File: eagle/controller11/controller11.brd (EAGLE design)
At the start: 36.8 x 64.8 mm, 62 parts, among them IC1 ILD213T, IC2 ILD213T, J2 FEMALE 2x3, Q2 200mA/50V, Q4 200mA/50V, Q5 200mA/50V, U3 MP2307, X1 1501_04, X2 ZX62D-B-5PA8

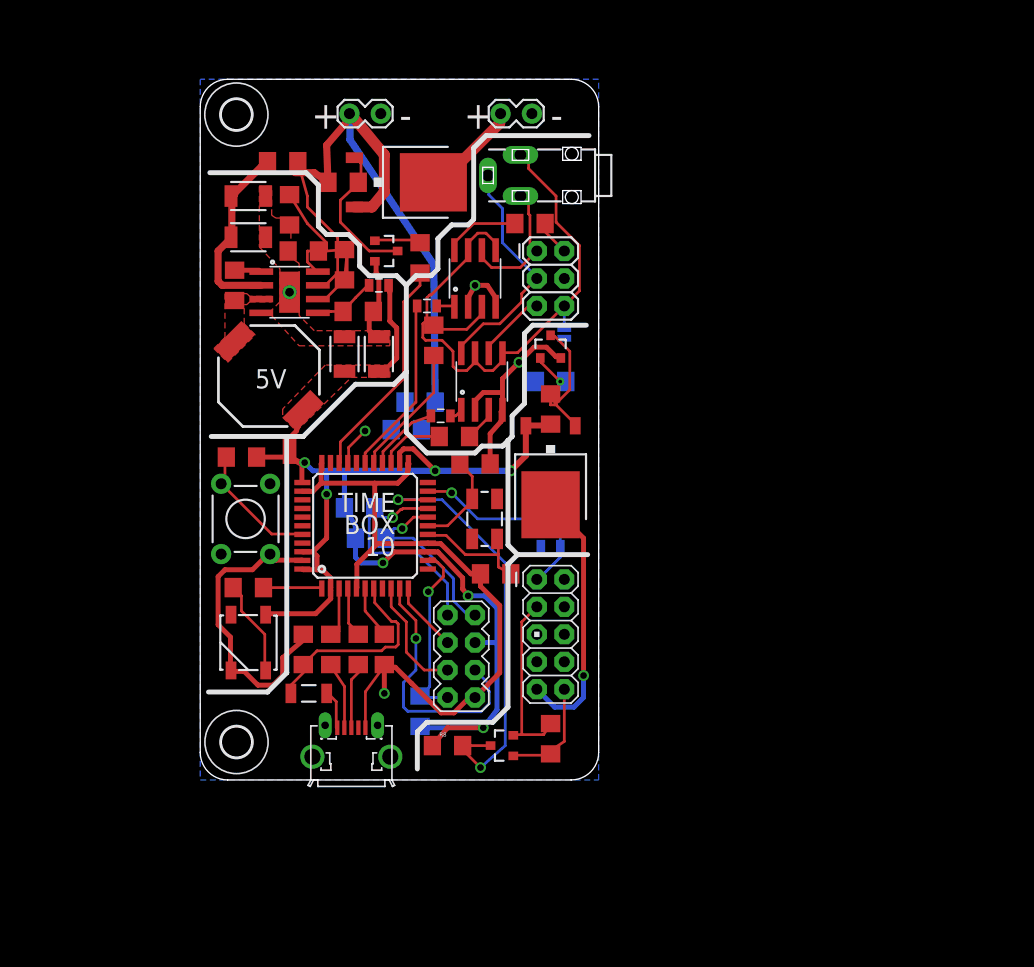
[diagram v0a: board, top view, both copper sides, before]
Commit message: controller11: new board layout
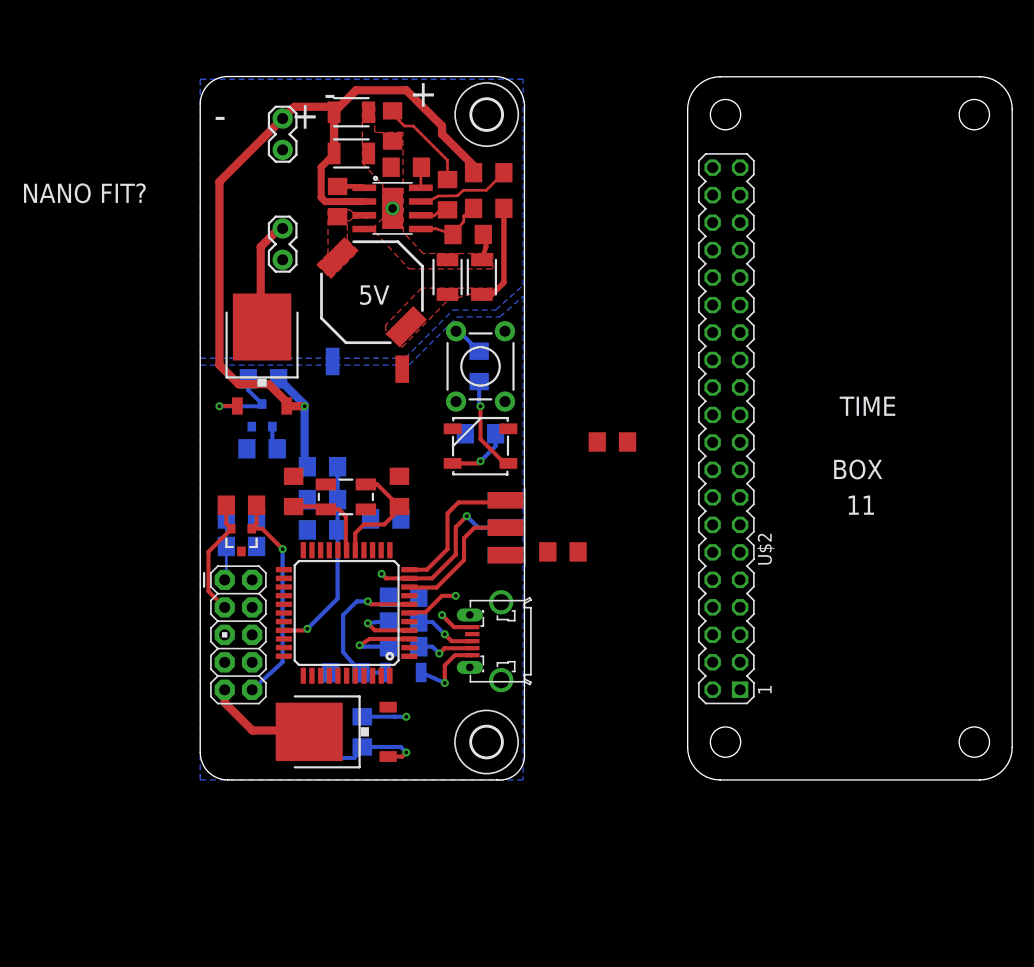
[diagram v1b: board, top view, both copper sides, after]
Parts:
- removed IC1, IC2: ILD213T, SparkFun-DiscreteSemi:SO08
- removed J2: FEMALE 2x3, SparkFun-Connectors:2X3
- removed J3: (no value), SparkFun-Connectors:2X4
- removed JP1: (no value), SparkFun-Passives:PAD-JUMPER-2-NO_YES_SILK
- removed R13, R14, R15, R16, R19: (no value), SparkFun-Passives:1206
- removed R18, R20: (no value), SparkFun-Passives:0805
- removed X1: 1501_04, con-lumberg:1501_05
- added C1, C6: 0.1uF, SparkFun-Capacitors:1206
- added SH2: SHORT-HT5, shorts:SHORT_TOP-50
- added U$1: AVR-ISP-6-EDGE, avr-6:6PAD_ISP
- added U$2: PIZERO_THROUGH_HOLE, pizero:PIZERO_THOUGH_HOLE
- R11, R12, R3: device SparkFun-Resistors:0805 -> SparkFun-Resistors:1206
- moved Q4 41.2 mm to (11.6, 4.45), flipped to the bottom, turned to 270 degrees
- moved R6 40.4 mm to (8.26, 4.45), turned to 90 degrees
- moved R7 35.8 mm to (3.81, 25.4), turned to 180 degrees
- moved R4 34.5 mm to (15.0, 4.45), flipped to the bottom, turned to 270 degrees
- moved Q5 30.7 mm to (3.81, 22.2), turned to 180 degrees
- moved Q3 30.7 mm to (12.6, 4.45), turned to 90 degrees
- moved J1 28.9 mm to (3.53, 13.4)
- moved R11 28.7 mm to (3.81, 21.6), turned to 0 degrees
- moved R12 28.7 mm to (3.81, 24.1), turned to 180 degrees
- moved D2 28.1 mm to (25.9, 30.9), turned to 180 degrees
- moved J9 26.5 mm to (7.62, 48.3), turned to 90 degrees
- moved S1 25.9 mm to (25.9, 38.2)
- moved R_LED 25.7 mm to (25.9, 32.0), flipped to the bottom
- moved R5 23.5 mm to (25.8, 38.2), flipped to the bottom, turned to 90 degrees
- moved H2 23.1 mm to (26.5, 61.5)
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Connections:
- removed net CAM3: R18.1, U$3.26
- removed net CAM4: R19.1, U$3.25
- removed net N$12: IC2.1, R18.2
- removed net N$13: IC2.3, R19.2
- removed net N$15: IC1.3, R15.2
- removed net N$16: J2.2, R13.2
- removed net N$18: IC1.8, R13.1
- removed net N$19: IC1.1, R20.2
- removed net N$31: IC1.6, J2.1, X1.3
- removed net N$32: IC2.8, J2.3, X1.2
- removed net N$33: IC2.6, J2.5
- removed net N$34: IC1.5, IC1.7, IC2.5, IC2.7, J2.6, JP1.2, X1.1
- removed net SCL: J3.2, R16.2, U$3.18
- removed net SDA: J3.1, R14.1, U$3.19
- new net FOO10: U$3.32
- new net FOO9: U$3.31
- new net GNDA: C15.1, C16.1, C17.1, C18.2, C19.1, R1.2, R2.2, SH2.1, U3.4, U3.BTM, U3.P$1
- net CAM1: no longer R20.1
- net CAM2: no longer R15.1
- net CAM_EN: now also U$3.25; no longer U$3.31
- net GND: now also C1.1, C6.2, SH2.2, U$1.GND; no longer C15.1, C16.1, C17.1, C18.2, C19.1, IC1.2, IC1.4, IC2.2, IC2.4, J3.8, JP1.1, R1.2, R2.2, U3.4, U3.BTM, U3.P$1
- net MISO: now also U$1.MISO; no longer J3.3
- net MOSI: now also U$1.MOSI; no longer J3.6
- net RST: now also U$1.RST; no longer J3.7
- net SCK: now also U$1.SCK; no longer J3.5
- net VCC: now also C1.2, U$1.VCC; no longer J3.4, R14.2, R16.1
- net VD_DIRECT: now also C6.1
- net ZERO_EN: now also U$3.26; no longer U$3.32
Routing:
- net GND: track 131.2 -> 3.26 mm, vias 3 -> 1
- net VCC: track 110.8 -> 13.0 mm, vias 7 -> 2
- net N$34: track 54.1 -> 0.00 mm
- net RX: track 41.7 -> 0.00 mm, vias 2 -> 0
- net N$32: track 22.1 -> 0.00 mm
- net SDA: track 21.2 -> 0.00 mm, vias 1 -> 0
- net CAM_EN: track 20.7 -> 0.00 mm
- net RST: track 17.4 -> 0.00 mm, vias 1 -> 0
- net SCL: track 17.1 -> 0.00 mm, vias 1 -> 0
- net CAM1: track 16.6 -> 0.00 mm
- net VD_DIRECT: track 3.64 -> 18.6 mm
- net ZERO_5V: track 24.5 -> 10.1 mm, vias 1 -> 0
- net N$31: track 13.0 -> 0.00 mm
- net CAM2: track 12.3 -> 0.00 mm
- net BATT_VCC: track 69.1 -> 80.7 mm, vias 0 -> 1
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- added copper zone on layer 1, net GNDA
- added copper zone on layer 16, net GNDA
- removed copper zone on layer 1, net GND
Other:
- board size 36.8 x 64.8 mm -> 30 x 65 mm
- board text added: "11"
- board text added: "NANO FIT?"
- board text removed: "10"

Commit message: controller11: nano fit
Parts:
- removed J7, J9: (no value), SparkFun-Connectors:1X02_LOCK
- added IC1: ILD213T, SparkFun-DiscreteSemi:SO08
- added JP1: (no value), SparkFun-Passives:PAD-JUMPER-2-NO_YES_SILK
- added R15, R20: (no value), SparkFun-Passives:1206
- added U$4, U$5: NANOFIT2, volzolib:NANOFIT2
- added X1: 1501_04, con-lumberg:1501_05
- S1: device SparkFun-Retired:TACTILE-PTH -> SparkFun-Retired:TACTILE-SWITCH-SMD
- moved C1 34.5 mm to (16.5, 4.32), turned to 90 degrees
- moved R5 22.2 mm to (4.19, 33.1), flipped to the top, turned to 0 degrees
- moved S1 22.1 mm to (3.81, 38.7), turned to 90 degrees
- moved R10 13.9 mm to (8.26, 44.3), flipped to the top, turned to 90 degrees
- moved RRST 12.2 mm to (22.9, 26.9)
- moved Q2 11.2 mm to (3.43, 44.6), flipped to the top, turned to 180 degrees
- moved D2 9.14 mm to (25.9, 40.0), turned to 0 degrees
- moved R8 8.92 mm to (8.64, 26.8), turned to 270 degrees
- moved R24 7.55 mm to (21.6, 61.7), turned to 270 degrees
- moved R_LED 7.11 mm to (25.9, 39.1), turned to 0 degrees
- moved R4 4.83 mm to (19.8, 4.45), turned to 90 degrees
- moved R11 3.56 mm to (3.81, 25.1)
- moved R12 3.56 mm to (3.81, 27.7)
- moved SH2 3.56 mm to (15.8, 38.7)
- moved VD1 3.10 mm to (13.1, 26.4)
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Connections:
- new net N$12: IC1.6, X1.2
- new net N$13: IC1.8, X1.3
- new net N$15: IC1.3, R15.2
- new net N$19: IC1.1, R20.2
- new net N$34: IC1.5, IC1.7, JP1.2, X1.1
- net BATT_VCC: now also U$4.P$1; no longer J7.2
- net CAM1: now also R20.1
- net CAM2: now also R15.1
- net CAM_OUT: now also U$5.P$1; no longer J9.2
- net GND: now also IC1.2, IC1.4, JP1.1, U$4.P$2, U$5.P$2; no longer J7.1, J9.1
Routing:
- net GND: track 3.26 -> 48.5 mm, vias 1 -> 2
- net BATT_VCC: track 80.7 -> 38.6 mm, vias 1 -> 0
- net VCC: track 13.0 -> 38.3 mm, vias 2 -> 1
- net N$13: track 0.00 -> 16.7 mm
- net N$34: track 0.00 -> 13.2 mm
- net N$3: track 12.9 -> 0.00 mm, vias 1 -> 0
- net N$1: track 8.55 -> 15.3 mm
- net N$12: track 0.00 -> 4.18 mm
- net CONV_5V: track 9.98 -> 13.6 mm
- net ZERO_RX: track 5.70 -> 9.26 mm
- net PB_BUCK_EN: track 8.68 -> 11.9 mm
- net RX: track 0.00 -> 2.65 mm, vias 0 -> 1
- net TX: track 0.00 -> 2.16 mm, vias 0 -> 1
- net VD_DIRECT: track 18.6 -> 16.8 mm
- net N$6: track 2.23 -> 3.94 mm
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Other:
- board text removed: "NANO FIT?"

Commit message: controller11: progress in routing
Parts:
- removed U$1: AVR-ISP-6-EDGE, avr-6:6PAD_ISP
- added J2: AVR_SPI_PRG_62X3_LOCK, SparkFun-Connectors:2X3_LOCK
- added J3: (no value), SparkFun-Connectors:2X4
- moved X1 33.0 mm to (-1.52, 34.0), turned to 90 degrees
- moved U$4 30.4 mm to (30.0, 54.1), turned to 180 degrees
- moved U$5 30.3 mm to (30.0, 46.2), turned to 180 degrees
- moved R_LED 22.4 mm to (20.8, 61.0), turned to 90 degrees
- moved D2 22.4 mm to (18.3, 61.1), turned to 180 degrees
- moved S1 22.4 mm to (26.2, 38.2)
- moved R5 21.8 mm to (26.0, 33.1)
- moved R20 21.0 mm to (13.0, 33.0), flipped to the bottom, turned to 90 degrees
- moved Q2 20.9 mm to (20.7, 32.9)
- moved R15 20.4 mm to (15.5, 33.0), flipped to the bottom, turned to 90 degrees
- moved Q1 19.3 mm to (24.0, 36.8)
- moved R9 19.3 mm to (24.1, 29.5)
- moved JP1 16.2 mm to (18.3, 41.9), turned to 180 degrees
- moved R10 14.5 mm to (20.4, 36.4), turned to 0 degrees
- moved SH2 11.2 mm to (4.62, 40.0)
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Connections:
- net BATT_VCC: now also U$4.P$2; no longer U$4.P$1
- net CAM_OUT: now also U$5.P$2; no longer U$5.P$1
- net GND: now also J2.6, U$4.P$1, U$5.P$1; no longer U$1.GND, U$4.P$2, U$5.P$2
- net MISO: now also J2.1; no longer U$1.MISO
- net MOSI: now also J2.4; no longer U$1.MOSI
- net RST: now also J2.5; no longer U$1.RST
- net SCK: now also J2.3; no longer U$1.SCK
- net VCC: now also J2.2; no longer U$1.VCC
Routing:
- net BATT_VCC: track 38.6 -> 78.0 mm, vias 0 -> 1
- net N$13: track 16.7 -> 0.00 mm
- net RST: track 0.00 -> 14.8 mm
- net N$19: track 0.00 -> 6.03 mm, vias 0 -> 1
- net N$7: track 5.72 -> 0.00 mm, vias 1 -> 0
- net VCC: track 38.3 -> 44.0 mm, vias 1 -> 0
- net N$15: track 0.00 -> 5.60 mm, vias 0 -> 1
- net MISO: track 12.9 -> 8.68 mm
- net N$12: track 4.18 -> 0.00 mm
- net N$20: track 4.95 -> 8.43 mm
- net N$3: track 0.00 -> 3.06 mm
- net CONV_5V: track 13.6 -> 16.7 mm
- net SCK: track 11.9 -> 14.8 mm
- net BTN: track 2.85 -> 0.00 mm
- net MOSI: track 15.4 -> 12.9 mm, vias 2 -> 1
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
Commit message: controller11: routing nearly finished
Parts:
- added H3: MOUNT-HOLE2.8, holes:2,8
- added J4: (no value), SparkFun-Connectors:1X02_LOCK
- moved J3 45.3 mm to (33.5, 23.4), turned to 270 degrees
- moved S1 36.5 mm to (14.6, 3.56), turned to 180 degrees
- moved X1 33.1 mm to (31.5, 32.0), turned to 270 degrees
- moved R5 29.3 mm to (20.2, 4.45), turned to 90 degrees
- moved R_LED 27.5 mm to (32.5, 36.1), flipped to the top
- moved D2 23.5 mm to (25.4, 38.7)
- moved JP1 12.2 mm to (25.4, 32.0), flipped to the bottom, turned to 0 degrees
- moved R9 11.9 mm to (15.7, 37.8), turned to 270 degrees
- moved Q4 8.42 mm to (4.45, 3.68), turned to 90 degrees
- moved R8 6.88 mm to (2.79, 23.0), flipped to the top, turned to 90 degrees
- moved R15 6.88 mm to (8.64, 32.5), flipped to the top
- moved R10 6.83 mm to (15.9, 41.5)
- moved Q2 6.83 mm to (16.1, 38.0)
- moved R7 5.11 mm to (3.30, 30.7)
- moved Q5 5.08 mm to (3.81, 27.3)
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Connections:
- new net SCL: J3.2, U$3.18
- new net SDA: J3.1, U$3.19
- net BATT_VCC: now also J4.1
- net BTN: now also U$3.32; no longer U$3.40
- net CAM1: now also U$3.27; no longer U$3.28
- net CAM2: now also U$3.28; no longer U$3.27
- net FOO10: now also U$3.26; no longer U$3.32
- net GND: now also J3.8, J4.2
- net MISO: now also J3.3
- net MOSI: now also J3.6
- net RST: now also J3.7
- net SCK: now also J3.5
- net VCC: now also J3.4
- net ZERO_EN: now also U$3.40; no longer U$3.26
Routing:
- net VCC: track 44.0 -> 139.4 mm, vias 0 -> 4
- net GND: track 49.9 -> 97.3 mm, vias 2 -> 5
- net CAM_EN: track 0.00 -> 33.2 mm, vias 0 -> 2
- net BTN: track 0.00 -> 27.2 mm
- net CAM1: track 0.00 -> 25.2 mm, vias 0 -> 2
- net CAM2: track 0.00 -> 21.2 mm, vias 0 -> 2
- net N$3: track 3.06 -> 23.9 mm, vias 0 -> 1
- net N$13: track 0.00 -> 14.4 mm
- net ZERO_EN: track 0.00 -> 11.1 mm
- net RX: track 2.65 -> 13.4 mm, vias 1 -> 0
- net TX: track 2.16 -> 11.6 mm
- net ZERO_TX: track 12.2 -> 16.8 mm
- net N$1: track 13.5 -> 9.47 mm
- net ZERO_3.3V: track 20.1 -> 23.6 mm
- net N$19: track 6.03 -> 2.71 mm, vias 1 -> 0
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
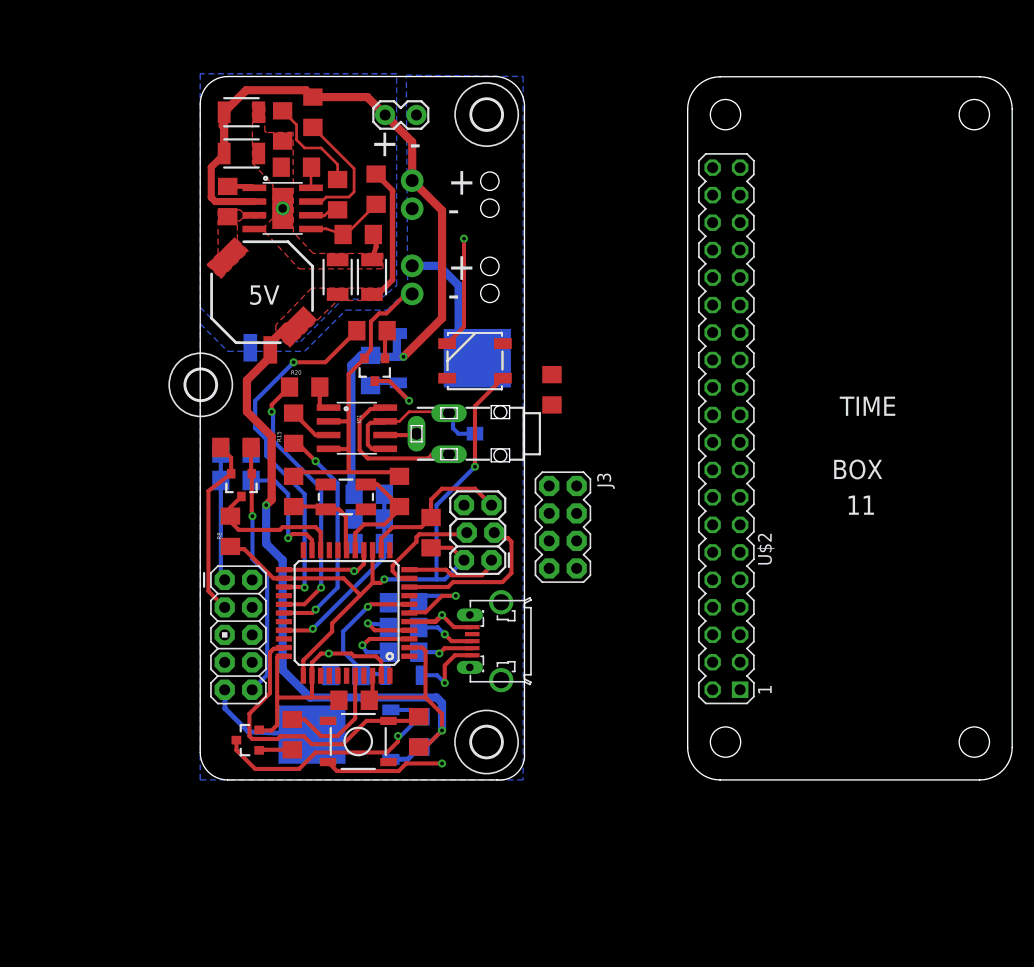
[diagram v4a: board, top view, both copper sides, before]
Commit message: controller11: routed all airwires
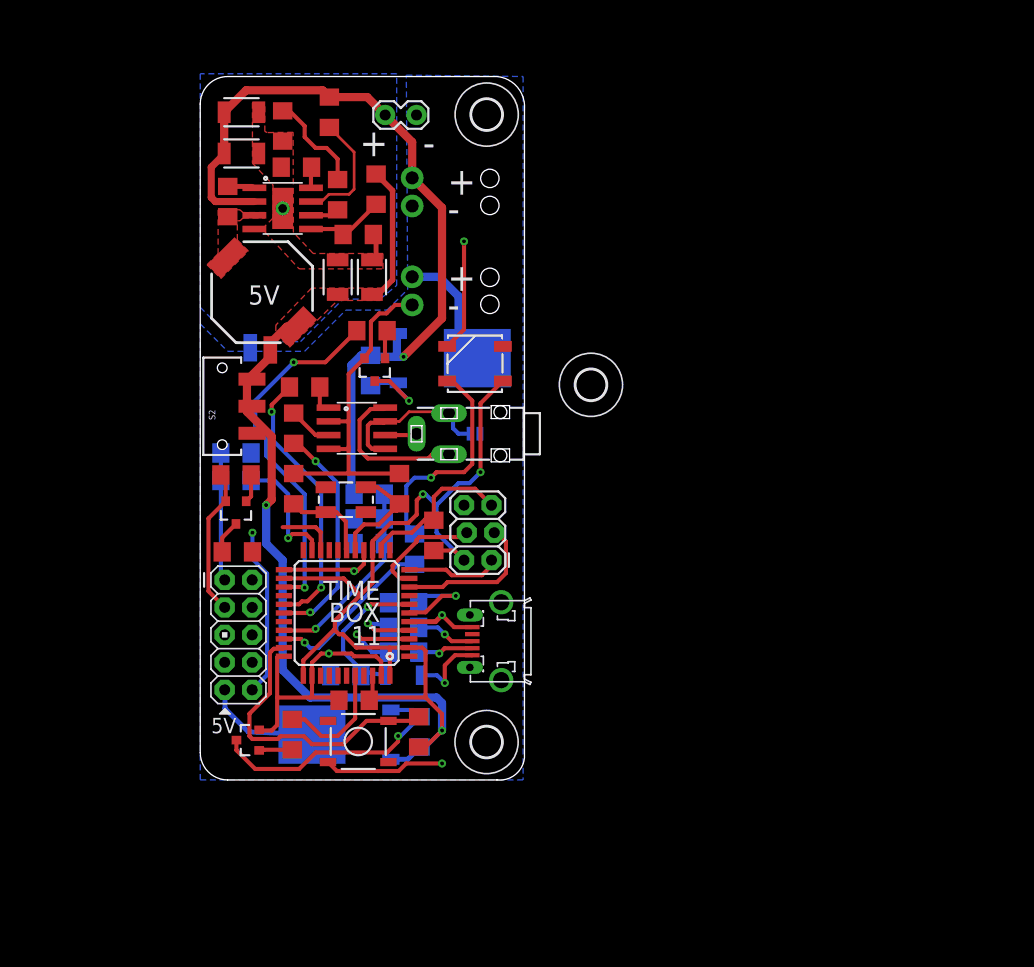
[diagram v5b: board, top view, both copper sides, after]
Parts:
- removed J3: (no value), SparkFun-Connectors:2X4
- removed U$2: PIZERO_THROUGH_HOLE, pizero:PIZERO_THOUGH_HOLE
- added S2: (no value), SparkFun-Electromechanical:SWITCH-SPDT-SMD
- moved H3 36.1 mm to (36.1, 36.5)
- moved R_LED 19.5 mm to (19.8, 21.3), flipped to the bottom
- moved Q5 2.59 mm to (3.30, 24.8)
- moved R7 2.54 mm to (3.30, 28.2)
- moved R8 2.01 mm to (3.43, 21.1), turned to 180 degrees
- moved R24 1.52 mm to (11.9, 61.7)
- moved U$5 1.02 mm to (30.0, 45.2)
- moved RRST 0.36 mm to (21.6, 22.6)
- moved U$4 0.25 mm to (30.0, 54.4)
- moved C4 0.25 mm to (8.64, 26.9)
- moved C5 0.25 mm to (18.4, 26.9)
- moved D2 0.25 mm to (25.4, 38.5)
- moved Y1 0.25 mm to (13.5, 25.9)
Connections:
- net FOO9: now also U$3.1; no longer U$3.31
- net GND: no longer J3.8
- net LED: now also U$3.31; no longer U$3.1
- net MISO: no longer J3.3
- net MOSI: no longer J3.6
- net RST: no longer J3.7
- net SCK: no longer J3.5
- net SCL: no longer J3.2
- net SDA: no longer J3.1
- net VCC: no longer J3.4
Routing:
- net N$7: track 0.00 -> 20.6 mm, vias 0 -> 1
- net LED: track 0.00 -> 15.9 mm, vias 0 -> 1
- net ZERO_3.3V: track 23.6 -> 18.3 mm
- net RX: track 13.4 -> 8.48 mm
- net VCC: track 139.4 -> 143.1 mm
- net ZERO_TX: track 16.8 -> 13.7 mm
- net N$4: track 7.33 -> 8.71 mm
- net BATT_VCC: track 76.9 -> 75.6 mm
- net SCK: track 14.8 -> 13.8 mm
- net CAM_OUT: track 13.1 -> 12.1 mm
- net N$29: track 3.62 -> 2.67 mm
- net GND: track 97.3 -> 98.1 mm
- net PB_BUCK_EN: track 11.9 -> 11.1 mm
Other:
- board text added: "VD1"
- board text added: "VD2"
